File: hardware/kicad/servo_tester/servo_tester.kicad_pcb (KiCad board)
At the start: 2 copper layers, 119 x 73.5 mm, 36 parts, among them J1 Servo 2, J2 Servo 3, J3 Servo 1, SW1 SW_Push - Select, SW2 SW_Push - Down, SW3 SW_Push - Up, SW4 HV (8,4V) / STD (5V), U1 INA3221, U2 Mini360

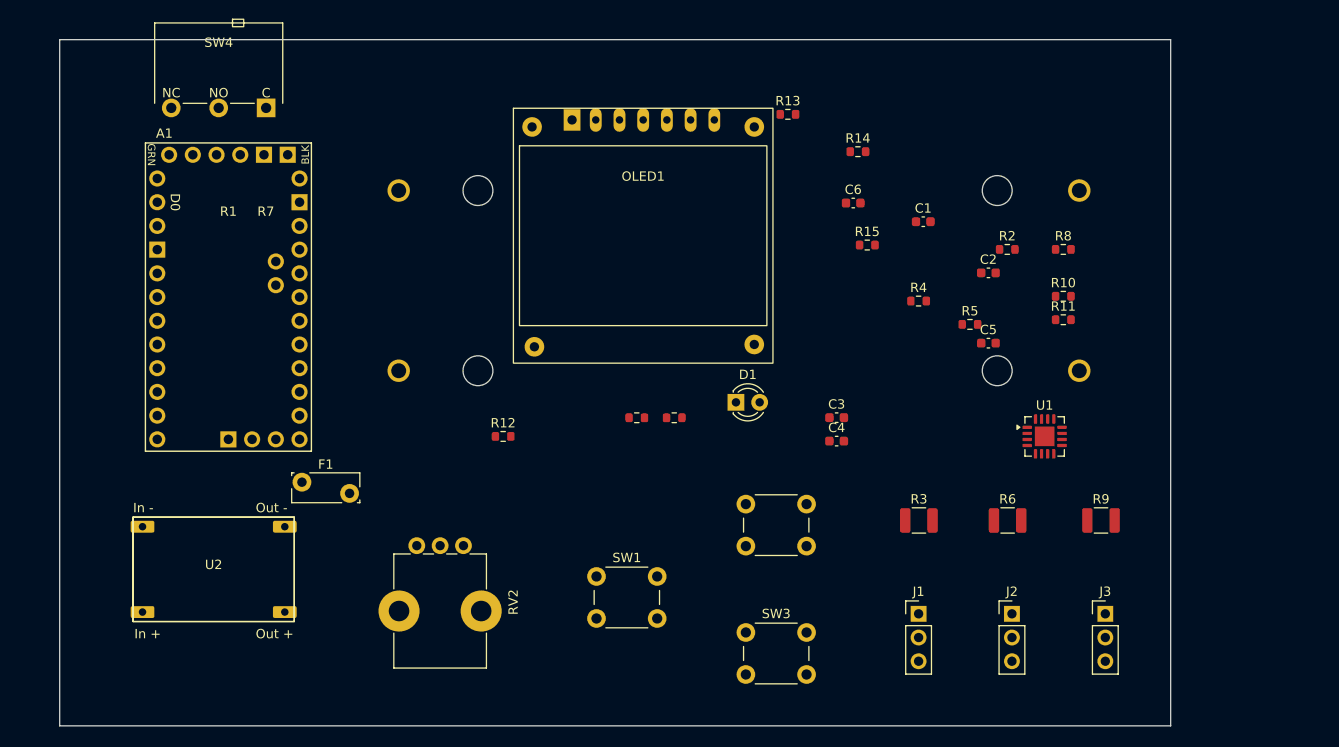
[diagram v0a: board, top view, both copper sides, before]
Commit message: Update OLED pin mapping and sync hardware files
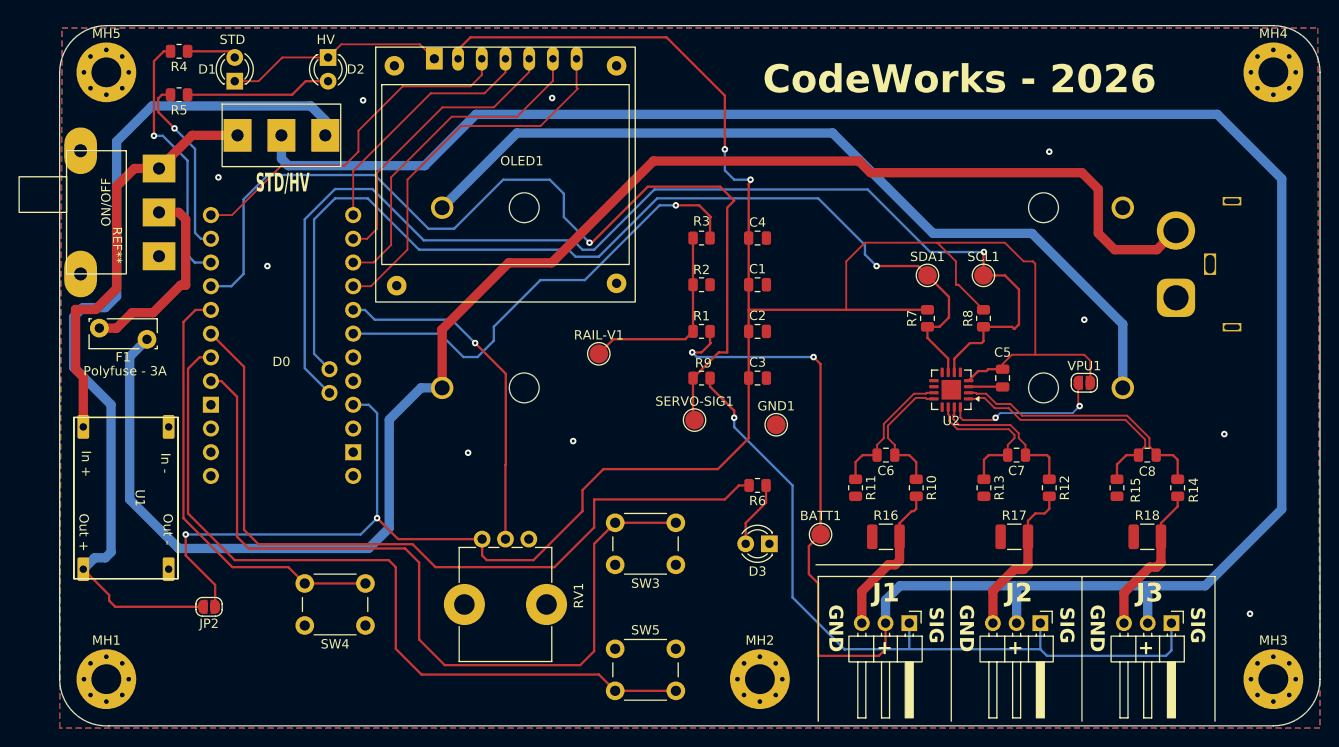
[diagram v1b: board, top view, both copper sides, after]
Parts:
- removed the SW4 at (111.9, 64.6)
- added BATT1: BATT, TestPoint:TestPoint_Pad_D2.0mm, F.Cu at (171.2, 110.2)
- added C1: 100nF, Capacitor_SMD:C_0805_2012Metric, F.Cu at (164.5, 83.5)
- added C2: 100nF, Capacitor_SMD:C_0805_2012Metric, F.Cu at (164.5, 88.5)
- added D1: STD, LED_THT:LED_D3.0mm, F.Cu at (108.5, 61.7)
- added D2: HV, LED_THT:LED_D3.0mm, F.Cu at (118.5, 59.2)
- added GND1: GND, TestPoint:TestPoint_Pad_D2.0mm, F.Cu at (166.5, 98.5)
- added J4: XT60PW-M, Connector_AMASS:AMASS_XT60IPW-M_1x03_P7.20mm_Horizontal, B.Cu at (209.3, 84.9)
- added JP2: 5V, Jumper:SolderJumper-2_P1.3mm_Open_RoundedPad1.0x1.5mm, F.Cu at (105.8, 118.0)
- added MH1: M3, MountingHole:MountingHole_3.2mm_M3_Pad_Via, F.Cu at (94.8, 125.8)
- added MH2: M3, MountingHole:MountingHole_3.2mm_M3_Pad_Via, F.Cu at (164.8, 125.8)
- added MH3: M3, MountingHole:MountingHole_3.2mm_M3_Pad_Via, F.Cu at (219.8, 125.8)
- added MH4: M3, MountingHole:MountingHole_3.2mm_M3_Pad_Via, F.Cu at (219.8, 60.8)
- added MH5: M3, MountingHole:MountingHole_3.2mm_M3_Pad_Via, F.Cu at (94.8, 60.8)
- added R3: 0R, Resistor_SMD:R_0805_2012Metric, F.Cu at (158.5, 78.5)
- added R4: 1K, Resistor_SMD:R_0805_2012Metric, F.Cu at (102.5, 58.5)
- added R5: 1K, Resistor_SMD:R_0805_2012Metric, F.Cu at (102.5, 63.1)
- added RAIL-V1: ~, TestPoint:TestPoint_Pad_D2.0mm, F.Cu at (147.5, 90.9)
- added SCL1: SCL, TestPoint:TestPoint_Pad_D2.0mm, F.Cu at (188.7, 82.5)
- added SDA1: SDA, TestPoint:TestPoint_Pad_D2.0mm, F.Cu at (182.7, 82.5)
- added SERVO-SIG1: SERVO-SIG, TestPoint:TestPoint_Pad_D2.0mm, F.Cu at (157.8, 98.0)
- added SW1: SS-12D11, CodeWorks-Essentials:SS-12D11, F.Cu at (100.4, 75.8)
- added SW2: STD / HV, CodeWorks-Essentials:SS-12D10, F.Cu at (113.5, 67.5)
- added VPU1: VPU, Jumper:SolderJumper-2_P1.3mm_Open_RoundedPad1.0x1.5mm, F.Cu at (199.5, 94.0)
- A1: footprint PCM_arduino-library:Clone_Pro_Mini_Socket -> CodeWorks-Essentials:Clone_Pro_Mini_Socket_No_PROG; moved to B.Cu
- C3: renamed from C4; footprint Capacitor_SMD:C_0603_1608Metric -> Capacitor_SMD:C_0805_2012Metric
- C4: renamed from C5; footprint Capacitor_SMD:C_0603_1608Metric -> Capacitor_SMD:C_0805_2012Metric
- C5: renamed from C6; footprint Capacitor_SMD:C_0603_1608Metric -> Capacitor_SMD:C_0805_2012Metric
- C6: renamed from C1; footprint Capacitor_SMD:C_0603_1608Metric -> Capacitor_SMD:C_0805_2012Metric
- C7: renamed from C2; footprint Capacitor_SMD:C_0603_1608Metric -> Capacitor_SMD:C_0805_2012Metric
- C8: renamed from C3; footprint Capacitor_SMD:C_0603_1608Metric -> Capacitor_SMD:C_0805_2012Metric
- D3: renamed from D1; value LED -> ALERT
- F1: value Polyfuse -> Polyfuse - 3A
- J1: renamed from J3; footprint Connector_PinHeader_2.54mm:PinHeader_1x03_P2.54mm_Vertical -> Connector_PinHeader_2.54mm:PinHeader_1x03_P2.54mm_Horizontal
- J2: renamed from J1; footprint Connector_PinHeader_2.54mm:PinHeader_1x03_P2.54mm_Vertical -> Connector_PinHeader_2.54mm:PinHeader_1x03_P2.54mm_Horizontal
- J3: renamed from J2; footprint Connector_PinHeader_2.54mm:PinHeader_1x03_P2.54mm_Vertical -> Connector_PinHeader_2.54mm:PinHeader_1x03_P2.54mm_Horizontal
- R1: renamed from R13; footprint Resistor_SMD:R_0603_1608Metric -> Resistor_SMD:R_0805_2012Metric
- R10: renamed from R2; footprint Resistor_SMD:R_0603_1608Metric -> Resistor_SMD:R_0805_2012Metric
- R11: renamed from R1; footprint Resistor_SMD:R_0603_1608Metric -> Resistor_SMD:R_0805_2012Metric
- R12: renamed from R4; footprint Resistor_SMD:R_0603_1608Metric -> Resistor_SMD:R_0805_2012Metric
- R13: renamed from R5; footprint Resistor_SMD:R_0603_1608Metric -> Resistor_SMD:R_0805_2012Metric
- R14: renamed from R7; footprint Resistor_SMD:R_0603_1608Metric -> Resistor_SMD:R_0805_2012Metric
- R15: renamed from R8; footprint Resistor_SMD:R_0603_1608Metric -> Resistor_SMD:R_0805_2012Metric
- R2: renamed from R14; footprint Resistor_SMD:R_0603_1608Metric -> Resistor_SMD:R_0805_2012Metric
- R6: renamed from R15; footprint Resistor_SMD:R_0603_1608Metric -> Resistor_SMD:R_0805_2012Metric
- R7: renamed from R10; footprint Resistor_SMD:R_0603_1608Metric -> Resistor_SMD:R_0805_2012Metric
- R8: renamed from R11; footprint Resistor_SMD:R_0603_1608Metric -> Resistor_SMD:R_0805_2012Metric
- R9: renamed from R12; footprint Resistor_SMD:R_0603_1608Metric -> Resistor_SMD:R_0805_2012Metric
- SW3: footprint Button_Switch_THT:SW_PUSH_6mm -> Button_Switch_THT:SW_PUSH_6mm_H8.5mm
- SW4: renamed from SW1; footprint Button_Switch_THT:SW_PUSH_6mm -> Button_Switch_THT:SW_PUSH_6mm_H8.5mm
- SW5: renamed from SW2; footprint Button_Switch_THT:SW_PUSH_6mm -> Button_Switch_THT:SW_PUSH_6mm_H8.5mm
- moved R14 54.4 mm to (209.5, 105.2), turned to -90 degrees
- moved C8 33.5 mm to (206.2, 101.8), turned to 180 degrees
- moved R6 28.3 mm to (164.5, 105.0), turned to 180 degrees
- moved R10 27.3 mm to (181.5, 105.2), turned to -90 degrees
- moved C4 27.2 mm to (164.5, 78.5)
- moved R15 26.2 mm to (203.0, 105.2), turned to -90 degrees
- moved C6 25.3 mm to (178.2, 101.8), turned to 180 degrees
- moved SW4 25.3 mm to (122.5, 120.0), turned to 180 degrees
- moved R1 25.0 mm to (158.5, 88.5)
- moved C5 24.6 mm to (190.8, 93.5), turned to -90 degrees
- moved R11 24.6 mm to (175.0, 105.2), turned to -90 degrees
- moved R12 24.4 mm to (195.8, 105.2), turned to -90 degrees
- moved F1 22.6 mm to (99.1, 89.3), turned to 180 degrees
- moved R9 22.2 mm to (158.5, 93.5), turned to 180 degrees
- moved R2 22.0 mm to (158.5, 83.5), turned to 180 degrees
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- renumbered R3 to R16, R6 to R17, R9 to R18, RV2 to RV1, U2 to U1, U1 to U2
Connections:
- net ALERT LED renamed /ALERT-LED
- net BTN - DOWN renamed /BTN-DOWN
- net BTN - SELECT renamed /BTN-SELECT
- net BTN - UP renamed /BTN-UP
- net Net-(U1-IN+1) renamed /IN+1
- net Net-(U1-IN+2) renamed /IN+2
- net Net-(U1-IN+3) renamed /IN+3
- net Net-(U1-IN-1) renamed /IN-1
- net Net-(U1-IN-2) renamed /IN-2
- net Net-(U1-IN-3) renamed /IN-3
- net POT renamed /POT
- net SCL renamed /SCL
- net SDA renamed /SDA
- A1 pad A1: RAIL V -> /RAIL V
- A1 pad D10: OLED CLK -> /OLED-MOSI
- A1 pad D11: OLED DC -> /OLED-RES
- A1 pad D12: OLED CS -> /OLED-DC
- A1 pad D13: OLED RST -> /OLED-CS
- A1 pad D6: SERVO-SIG -> /SERVO
- A1 pad D7: unconnected-(A1-PadD7) -> /STD
- A1 pad D8: unconnected-(A1-PadD8) -> /HV
- A1 pad D9: OLED MOSI -> /OLED-SCK
- J1 pad 1: SERVO-SIG -> /SERVO-SIG
- J1 pad 3: GND -> Net-(J1-Pin_3)
- J2 pad 1: SERVO-SIG -> /SERVO-SIG
- J2 pad 3: GND -> Net-(J2-Pin_3)
- J3 pad 1: SERVO-SIG -> /SERVO-SIG
- J3 pad 3: GND -> Net-(J3-Pin_3)
- OLED1 pad 3: OLED CLK -> /OLED-SCK
- OLED1 pad 4: OLED MOSI -> /OLED-MOSI
- OLED1 pad 5: OLED RST -> /OLED-RES
- OLED1 pad 6: OLED DC -> /OLED-DC
- OLED1 pad 7: OLED CS -> /OLED-CS
- R1 pad 1: RAIL V -> Net-(R1-Pad1)
- R10 pad 2: GND -> Net-(J1-Pin_3)
- R12 pad 2: GND -> Net-(J2-Pin_3)
- R14 pad 2: GND -> Net-(J3-Pin_3)
- R16 pad 2: GND -> Net-(J1-Pin_3)
- R17 pad 2: GND -> Net-(J2-Pin_3)
- R18 pad 2: GND -> Net-(J3-Pin_3)
- R2 pad 2: RAIL V -> Net-(R1-Pad1)
- R9 pad 1: SERVO-SIG -> /SERVO-SIG
- R9 pad 2: SERVO-SIG -> /SERVO
- U1 pad 4: +5V -> Net-(JP2-B)
- U2 pad 16: +5V -> Net-(U2-VPU)
- U2 pad 4: unconnected-(U1-VS-Pad4) -> +5V
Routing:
- net +BATT: track 0.00 -> 267.8 mm, vias 0 -> 2
- net +5V: track 0.00 -> 248.2 mm, vias 0 -> 4
- net Net-(J4-N): track 0.00 -> 167.4 mm
- net /SCL: track 0.00 -> 123.6 mm, vias 0 -> 1
- net /SDA: track 0.00 -> 106.5 mm, vias 0 -> 1
- net /SERVO: track 0.00 -> 103.5 mm, vias 0 -> 1
- net Net-(JP2-B): track 0.00 -> 93.7 mm
- net Net-(BT1-Pad1-): track 0.00 -> 91.5 mm
- net /BTN-UP: track 0.00 -> 89.1 mm
- net /BTN-DOWN: track 0.00 -> 83.7 mm
- net /ALERT-LED: track 0.00 -> 83.6 mm
- net /SERVO-SIG: track 0.00 -> 78.9 mm, vias 0 -> 1
- net /RAIL V: track 0.00 -> 49.8 mm, vias 0 -> 1
- net /BTN-SELECT: track 0.00 -> 46.9 mm
- net Net-(U1-IN+): track 0.00 -> 44.4 mm
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- added copper zone on B.Cu, net GND
- added copper zone on F.Cu, net GND
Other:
- board size 119 x 73.5 mm -> 135 x 75 mm
- rule pad_to_mask_clearance: 0 -> 0.1
- board text added: "+"
- board text added: "2X18650"
- board text added: "CodeWorks - 2026"
- board text added: "GND"
- board text added: "SERVO TESTER"
- board text added: "SIG"
- board text added: "STD/HV"
